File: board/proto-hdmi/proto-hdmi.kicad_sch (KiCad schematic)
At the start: 38 parts, among them J1 Conn_02x17_Odd_Even, J2 HDMI_A_1.4

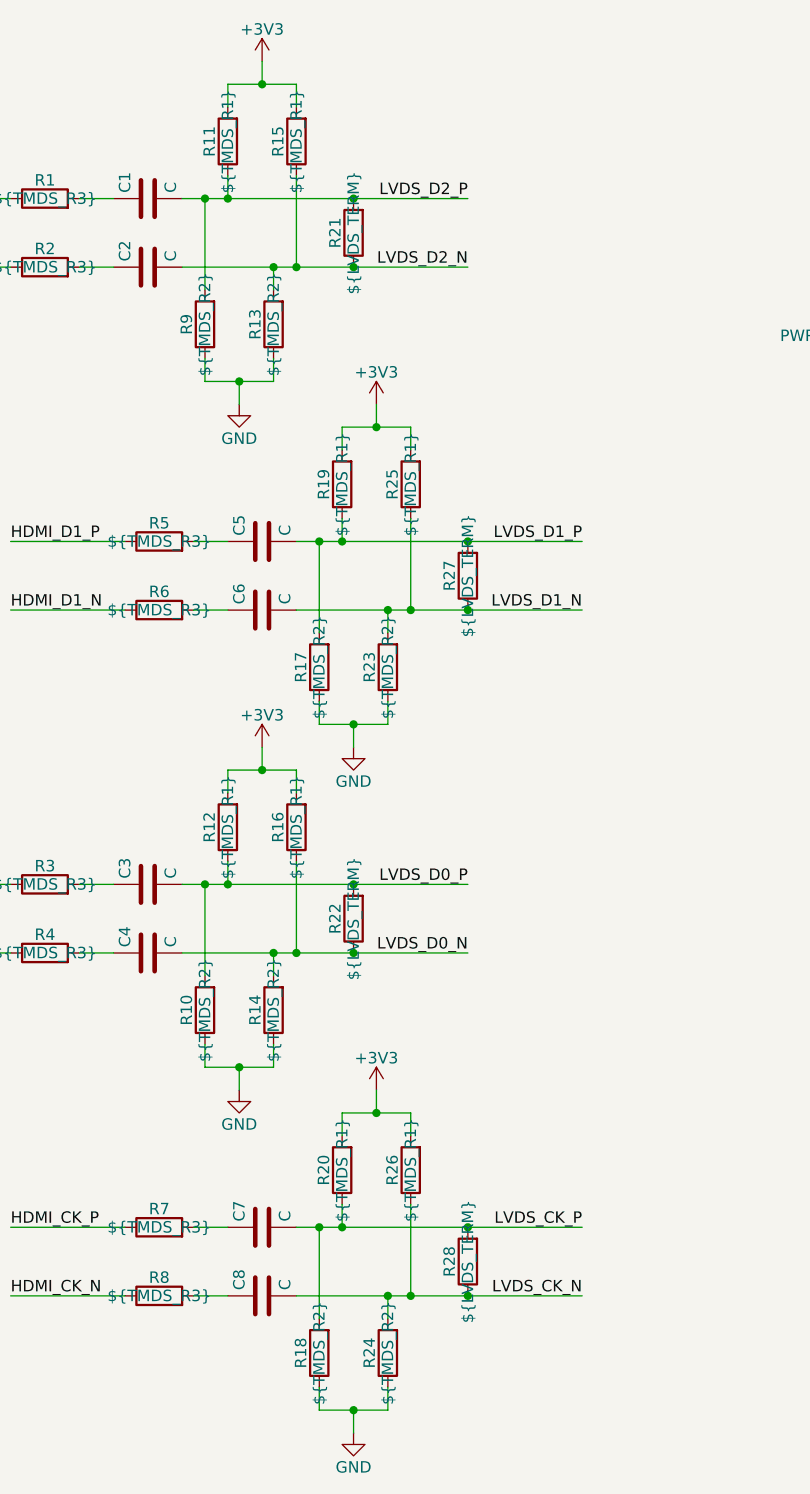
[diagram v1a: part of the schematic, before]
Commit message: Remove extraneous LVDS termination resistors.
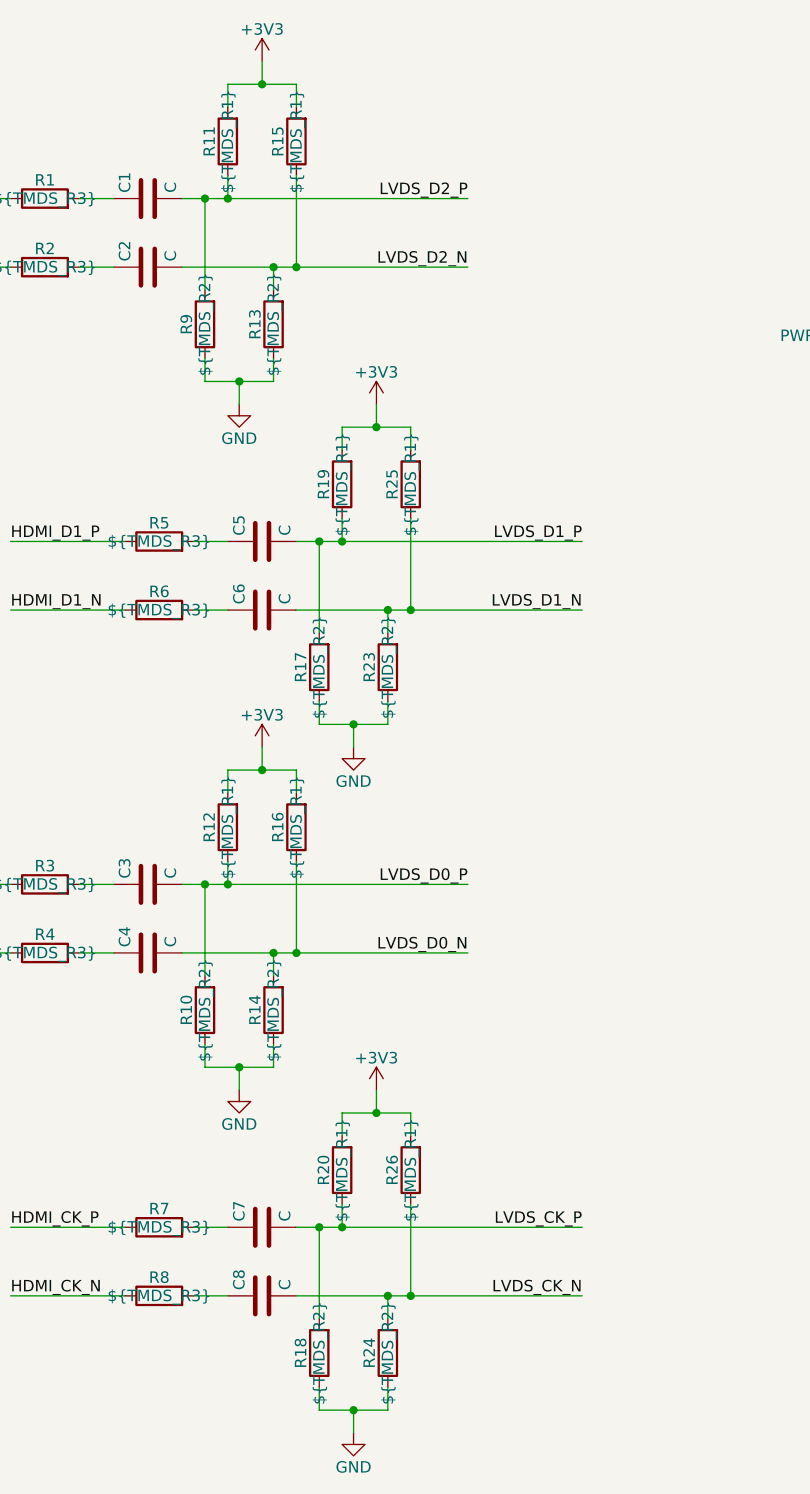
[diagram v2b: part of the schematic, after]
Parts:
- removed R21, R22, R27, R28: ${LVDS_TERM}, Resistor_SMD:R_0402_1005Metric, symbol Device:R
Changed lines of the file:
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@@
     (comment 1 "https://github.com/Elemecca/1240pi")
   )
-  (junction (at 152.4 83.82) (diameter 0) (color 0 0 0 0)
-  )
-  (junction (at 152.4 152.4) (diameter 0) (color 0 0 0 0)
-  )
   (junction (at 142.24 63.5) (diameter 0) (color 0 0 0 0)
   )
@@
   (junction (at 143.51 160.02) (diameter 0) (color 0 0 0 0)
   )
-  (junction (at 139.7 121.92) (diameter 0) (color 0 0 0 0)
-  )
   (junction (at 123.19 38.1) (diameter 0) (color 0 0 0 0)
   )
@@
   (junction (at 138.43 76.2) (diameter 0) (color 0 0 0 0)
   )
-  (junction (at 139.7 38.1) (diameter 0) (color 0 0 0 0)
-  )
   (junction (at 135.89 76.2) (diameter 0) (color 0 0 0 0)
   )
@@
   (junction (at 139.7 172.72) (diameter 0) (color 0 0 0 0)
   )
-  (junction (at 152.4 76.2) (diameter 0) (color 0 0 0 0)
-  )
   (junction (at 123.19 114.3) (diameter 0) (color 0 0 0 0)
   )
   (junction (at 139.7 96.52) (diameter 0) (color 0 0 0 0)
   )
-  (junction (at 139.7 114.3) (diameter 0) (color 0 0 0 0)
-  )
   (junction (at 207.01 59.69) (diameter 0) (color 0 0 0 0)
   )
@@
   (junction (at 138.43 152.4) (diameter 0) (color 0 0 0 0)
   )
-  (junction (at 152.4 160.02) (diameter 0) (color 0 0 0 0)
-  )
   (junction (at 44.45 106.68) (diameter 0) (color 0 0 0 0)
   )
   (junction (at 36.83 106.68) (diameter 0) (color 0 0 0 0)
-  )
-  (junction (at 139.7 45.72) (diameter 0) (color 0 0 0 0)
   )
   (junction (at 39.37 106.68) (diameter 0) (color 0 0 0 0)
@@
     (stroke (width 0) (type default) (color 0 0 0 0))
   )
-  (wire (pts (xy 139.7 121.92) (xy 152.4 121.92))
+  (wire (pts (xy 133.35 121.92) (xy 152.4 121.92))
     (stroke (width 0) (type default) (color 0 0 0 0))
   )
@@
     (stroke (width 0) (type default) (color 0 0 0 0))
   )
-  (wire (pts (xy 152.4 83.82) (xy 165.1 83.82))
+  (wire (pts (xy 146.05 83.82) (xy 165.1 83.82))
     (stroke (width 0) (type default) (color 0 0 0 0))
   )
@@
     (stroke (width 0) (type default) (color 0 0 0 0))
   )
-  (wire (pts (xy 133.35 121.92) (xy 139.7 121.92))
-    (stroke (width 0) (type default) (color 0 0 0 0))
-  )
   (wire (pts (xy 138.43 149.86) (xy 138.43 152.4))
     (stroke (width 0) (type default) (color 0 0 0 0))
@@
     (stroke (width 0) (type default) (color 0 0 0 0))
   )
-  (wire (pts (xy 152.4 152.4) (xy 165.1 152.4))
-    (stroke (width 0) (type default) (color 0 0 0 0))
-  )
   (wire (pts (xy 146.05 63.5) (xy 146.05 66.04))
     (stroke (width 0) (type default) (color 0 0 0 0))
   )
-  (wire (pts (xy 139.7 38.1) (xy 152.4 38.1))
+  (wire (pts (xy 125.73 38.1) (xy 152.4 38.1))
     (stroke (width 0) (type default) (color 0 0 0 0))
   )
@@
     (stroke (width 0) (type default) (color 0 0 0 0))
   )
-  (wire (pts (xy 146.05 160.02) (xy 152.4 160.02))
+  (wire (pts (xy 146.05 160.02) (xy 165.1 160.02))
     (stroke (width 0) (type default) (color 0 0 0 0))
   )
@@
     (stroke (width 0) (type default) (color 0 0 0 0))
   )
-  (wire (pts (xy 139.7 114.3) (xy 152.4 114.3))
+  (wire (pts (xy 125.73 114.3) (xy 152.4 114.3))
     (stroke (width 0) (type default) (color 0 0 0 0))
   )
@@
     (stroke (width 0) (type default) (color 0 0 0 0))
   )
-  (wire (pts (xy 125.73 38.1) (xy 139.7 38.1))
-    (stroke (width 0) (type default) (color 0 0 0 0))
-  )
   (wire (pts (xy 135.89 152.4) (xy 138.43 152.4))
     (stroke (width 0) (type default) (color 0 0 0 0))
@@
     (stroke (width 0) (type default) (color 0 0 0 0))
   )
-  (wire (pts (xy 146.05 83.82) (xy 152.4 83.82))
-    (stroke (width 0) (type default) (color 0 0 0 0))
-  )
   (wire (pts (xy 135.89 76.2) (xy 135.89 86.36))
     (stroke (width 0) (type default) (color 0 0 0 0))
@@
     (stroke (width 0) (type default) (color 0 0 0 0))
   )
-  (wire (pts (xy 138.43 76.2) (xy 152.4 76.2))
-    (stroke (width 0) (type default) (color 0 0 0 0))
-  )
   (wire (pts (xy 215.9 57.15) (xy 215.9 59.69))
     (stroke (width 0) (type default) (color 0 0 0 0))
@@
     (stroke (width 0) (type default) (color 0 0 0 0))
   )
-  (wire (pts (xy 152.4 160.02) (xy 165.1 160.02))
-    (stroke (width 0) (type default) (color 0 0 0 0))
-  )
   (wire (pts (xy 41.91 106.68) (xy 39.37 106.68))
     (stroke (width 0) (type default) (color 0 0 0 0))
@@
     (stroke (width 0) (type default) (color 0 0 0 0))
   )
-  (wire (pts (xy 133.35 45.72) (xy 139.7 45.72))
-    (stroke (width 0) (type default) (color 0 0 0 0))
-  )
   (wire (pts (xy 196.85 83.82) (xy 215.9 83.82))
     (stroke (width 0) (type default) (color 0 0 0 0))
@@
     (stroke (width 0) (type default) (color 0 0 0 0))
   )
-  (wire (pts (xy 138.43 152.4) (xy 152.4 152.4))
+  (wire (pts (xy 138.43 152.4) (xy 165.1 152.4))
     (stroke (width 0) (type default) (color 0 0 0 0))
   )
@@
     (stroke (width 0) (type default) (color 0 0 0 0))
   )
-  (wire (pts (xy 152.4 76.2) (xy 165.1 76.2))
+  (wire (pts (xy 138.43 76.2) (xy 165.1 76.2))
     (stroke (width 0) (type default) (color 0 0 0 0))
   )
@@
     (stroke (width 0) (type default) (color 0 0 0 0))
   )
-  (wire (pts (xy 125.73 114.3) (xy 139.7 114.3))
-    (stroke (width 0) (type default) (color 0 0 0 0))
-  )
   (wire (pts (xy 196.85 96.52) (xy 215.9 96.52))
     (stroke (width 0) (type default) (color 0 0 0 0))
@@
     (stroke (width 0) (type default) (color 0 0 0 0))
   )
-  (wire (pts (xy 139.7 45.72) (xy 152.4 45.72))
+  (wire (pts (xy 133.35 45.72) (xy 152.4 45.72))
     (stroke (width 0) (type default) (color 0 0 0 0))
   )
@@
     (pin "2")
   )
-  (symbol (lib_id "Device:R") (at 139.7 118.11 180) (unit 1)
-    (in_bom yes) (on_board yes)
-    (property "Reference" "R22" (id 0) (at 137.668 118.11 90))
-    (property "Value" "${LVDS_TERM}" (id 1) (at 139.7 118.11 90))
-    (property "Footprint" "Resistor_SMD:R_0402_1005Metric" (id 2) (at 141.478 118.11 90)
-      (effects (font (size 1.27 1.27)) hide)
-    )
-    (property "Datasheet" "~" (id 3) (at 139.7 118.11 0)
-      (effects (font (size 1.27 1.27)) hide)
-    )
-    (pin "1")
-    (pin "2")
-  )
   (symbol (lib_id "Device:R") (at 135.89 90.17 180) (unit 1)
     (in_bom yes) (on_board yes)
@@
     (pin "1")
   )
-  (symbol (lib_id "Device:R") (at 152.4 80.01 180) (unit 1)
-    (in_bom yes) (on_board yes)
-    (property "Reference" "R27" (id 0) (at 150.368 80.01 90))
-    (property "Value" "${LVDS_TERM}" (id 1) (at 152.4 80.01 90))
-    (property "Footprint" "Resistor_SMD:R_0402_1005Metric" (id 2) (at 154.178 80.01 90)
-      (effects (font (size 1.27 1.27)) hide)
-    )
-    (property "Datasheet" "~" (id 3) (at 152.4 80.01 0)
-      (effects (font (size 1.27 1.27)) hide)
-    )
-    (pin "1")
-    (pin "2")
-  )
   (symbol (lib_id "Device:R") (at 105.41 45.72 90) (unit 1)
     (in_bom yes) (on_board yes)
@@
     )
     (property "Datasheet" "~" (id 3) (at 129.54 83.82 0)
-      (effects (font (size 1.27 1.27)) hide)
-    )
-    (pin "1")
-    (pin "2")
-  )
-  (symbol (lib_id "Device:R") (at 139.7 41.91 180) (unit 1)
-    (in_bom yes) (on_board yes)
-    (property "Reference" "R21" (id 0) (at 137.668 41.91 90))
-    (property "Value" "${LVDS_TERM}" (id 1) (at 139.7 41.91 90))
-    (property "Footprint" "Resistor_SMD:R_0402_1005Metric" (id 2) (at 141.478 41.91 90)
-      (effects (font (size 1.27 1.27)) hide)
-    )
-    (property "Datasheet" "~" (id 3) (at 139.7 41.91 0)
       (effects (font (size 1.27 1.27)) hide)
     )
@@
     )
     (pin "1")
-  )
-  (symbol (lib_id "Device:R") (at 152.4 156.21 180) (unit 1)
-    (in_bom yes) (on_board yes)
-    (property "Reference" "R28" (id 0) (at 150.368 156.21 90))
-    (property "Value" "${LVDS_TERM}" (id 1) (at 152.4 156.21 90))
-    (property "Footprint" "Resistor_SMD:R_0402_1005Metric" (id 2) (at 154.178 156.21 90)
-      (effects (font (size 1.27 1.27)) hide)
-    )
-    (property "Datasheet" "~" (id 3) (at 152.4 156.21 0)
-      (effects (font (size 1.27 1.27)) hide)
-    )
-    (pin "1")
-    (pin "2")
   )
   (symbol (lib_id "Connector_Generic:Conn_02x17_Odd_Even") (at 220.98 83.82 0) (unit 1)
@@
       (reference "R20") (unit 1) (value "${TMDS_R1}") (footprint "Resistor_SMD:R_0402_1005Metric")
     )
-    (path "/4042c566-dbe0-4fcc-a8e6-2f9abdb810bb"
-      (reference "R21") (unit 1) (value "${LVDS_TERM}") (footprint "Resistor_SMD:R_0402_1005Metric")
-    )
-    (path "/104e9296-e4eb-4e51-9155-4c6635c6dad8"
-      (reference "R22") (unit 1) (value "${LVDS_TERM}") (footprint "Resistor_SMD:R_0402_1005Metric")
-    )
     (path "/3ac8a9ee-2153-4f97-8d54-eee8368f298d"
       (reference "R23") (unit 1) (value "${TMDS_R2}") (footprint "Resistor_SMD:R_0402_1005Metric")
@@
       (reference "R26") (unit 1) (value "${TMDS_R1}") (footprint "Resistor_SMD:R_0402_1005Metric")
     )
-    (path "/2095c295-4164-4ab7-b0cf-247827021489"
-      (reference "R27") (unit 1) (value "${LVDS_TERM}") (footprint "Resistor_SMD:R_0402_1005Metric")
-    )
-    (path "/782a149a-c296-4cfa-8045-5d14501481ec"
-      (reference "R28") (unit 1) (value "${LVDS_TERM}") (footprint "Resistor_SMD:R_0402_1005Metric")
-    )
-  )
+  )

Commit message: Add labels to HDMI board.
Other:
- title: HDMI Adapter for Lattice ICE40HX8K-B-EVN -> HDMI Expansion for Olimex ICE40HX8K-EVB
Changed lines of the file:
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@@
   (paper "USLetter")
   (title_block
-    (title "HDMI Adapter for Lattice ICE40HX8K-B-EVN")
+    (title "HDMI Expansion for Olimex ICE40HX8K-EVB")
     (date "2022-04-19")
-    (rev "1.0")
+    (rev "0.1")
     (company "© 2022 Sam Hanes, licensed under CERN-OHL-P v2")
     (comment 1 "https://github.com/Elemecca/1240pi")

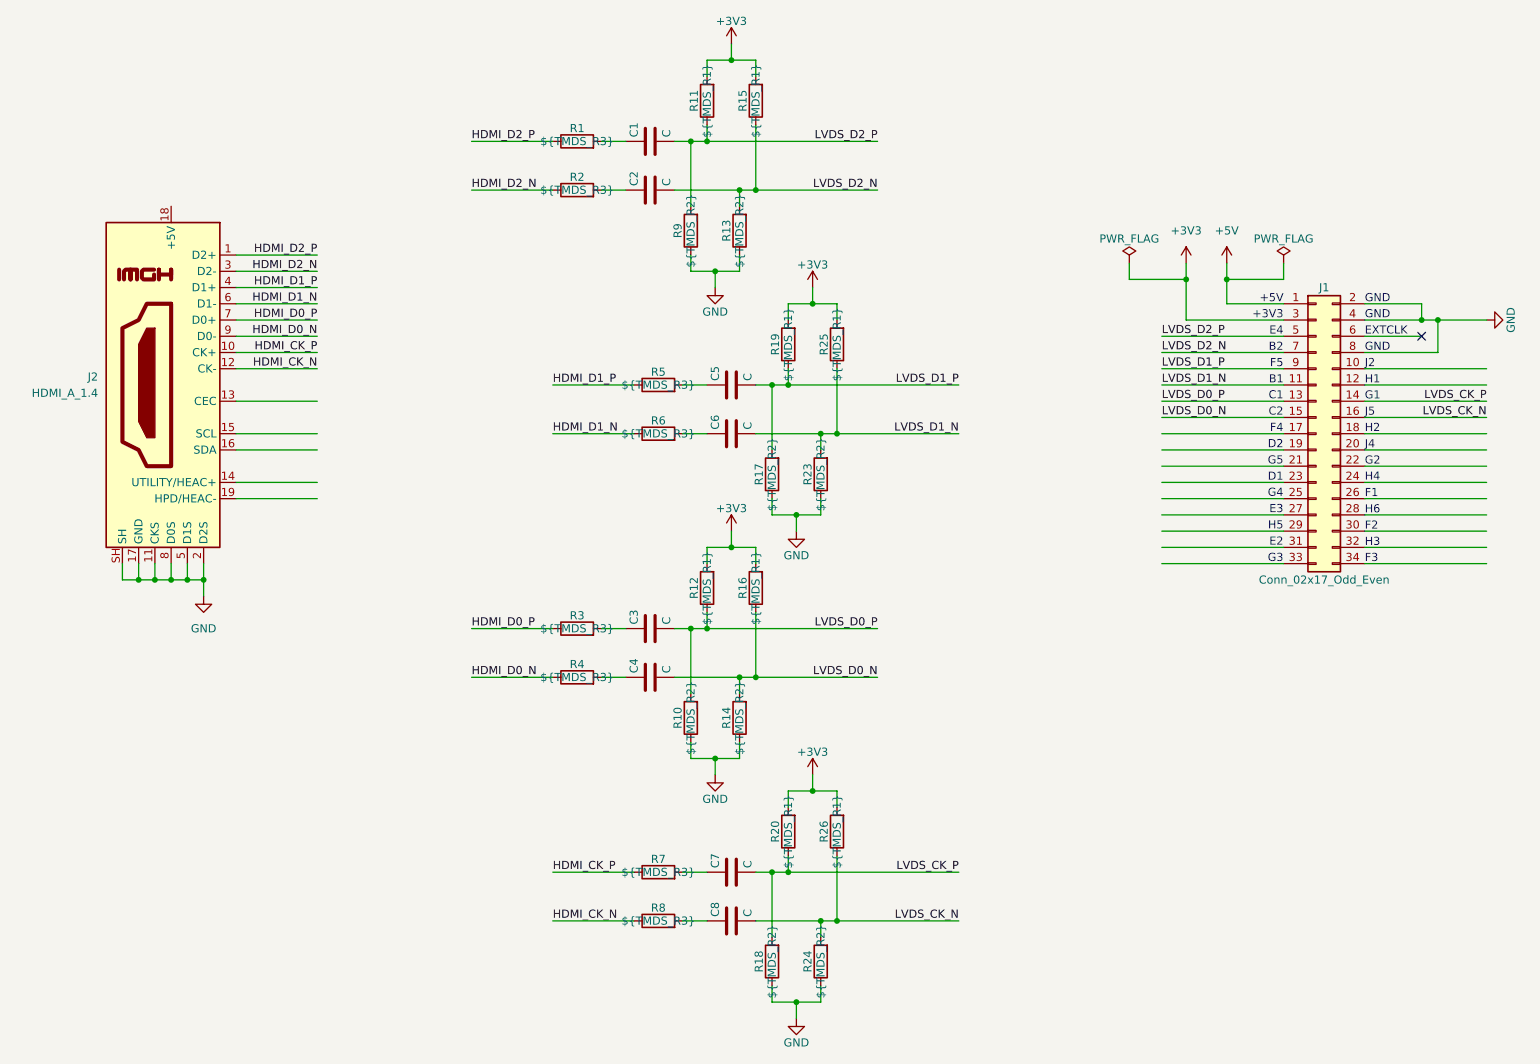
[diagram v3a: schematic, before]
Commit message: Add and route non-TMDS lines for sink port.
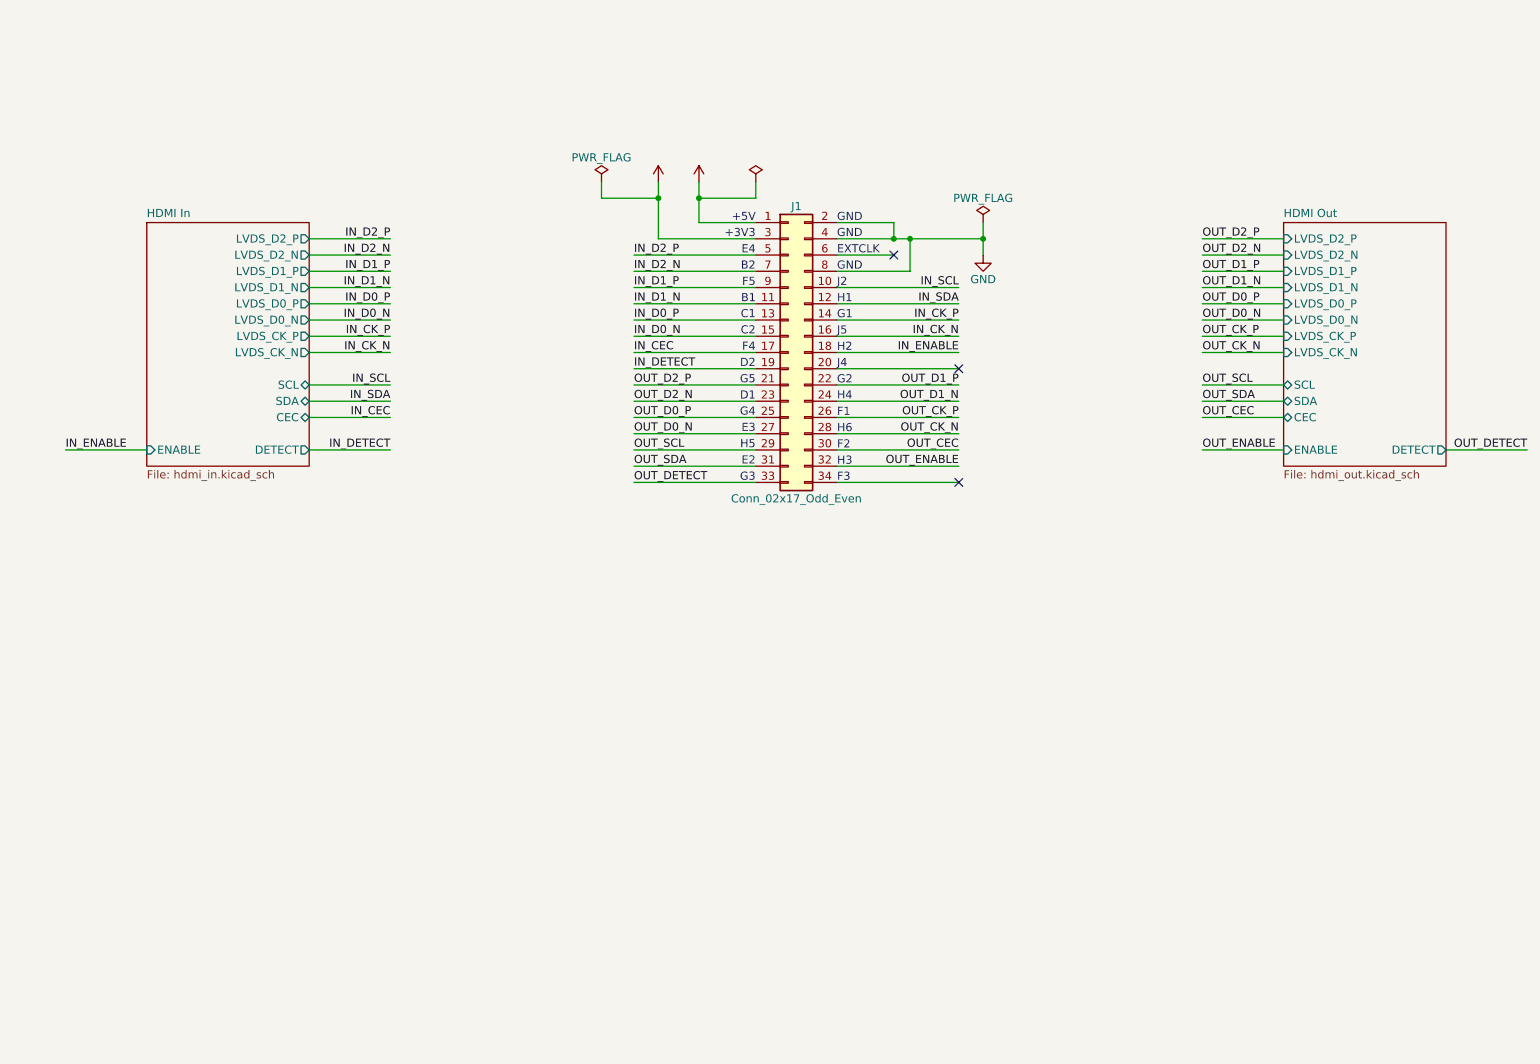
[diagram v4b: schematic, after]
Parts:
- removed C1, C2, C3, C4, C5, C6, C7, C8: C, Capacitor_SMD:C_0402_1005Metric, symbol Device:C
- removed J2: HDMI_A_1.4, 0Local:CNC_2000-1-2-41-00-BK, symbol Connector:HDMI_A_1.4
- removed R1, R2, R3, R4, R5, R6, R7, R8: ${TMDS_R3}, Resistor_SMD:R_0402_1005Metric, symbol Device:R
- removed R10, R13, R14, R17, R18, R23, R24, R9: ${TMDS_R2}, Resistor_SMD:R_0402_1005Metric, symbol Device:R
- removed R11, R12, R15, R16, R19, R20, R25, R26: ${TMDS_R1}, Resistor_SMD:R_0402_1005Metric, symbol Device:R
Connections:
- net IN_SCL: now reaches J1.10 (Pin_10)
- net IN_SDA: now reaches J1.12 (Pin_12)
- net IN_CEC: now reaches J1.17 (Pin_17)
- net IN_ENABLE: now reaches J1.18 (Pin_18)
- net IN_DETECT: now reaches J1.19 (Pin_19)
- net OUT_D2_P: now reaches J1.21 (Pin_21)
- net OUT_D1_P: now reaches J1.22 (Pin_22)
- net OUT_D2_N: now reaches J1.23 (Pin_23)
- net OUT_D1_N: now reaches J1.24 (Pin_24)
- net OUT_D0_P: now reaches J1.25 (Pin_25)
- net OUT_CK_P: now reaches J1.26 (Pin_26)
- net OUT_D0_N: now reaches J1.27 (Pin_27)
- net OUT_CK_N: now reaches J1.28 (Pin_28)
- net OUT_SCL: now reaches J1.29 (Pin_29)
- net OUT_CEC: now reaches J1.30 (Pin_30)
- net OUT_SDA: now reaches J1.31 (Pin_31)
- net OUT_ENABLE: now reaches J1.32 (Pin_32)
- net OUT_DETECT: now reaches J1.33 (Pin_33)
- net LVDS_CK_N renamed IN_CK_N
- net LVDS_CK_P renamed IN_CK_P
- net LVDS_D0_N renamed IN_D0_N
- net LVDS_D0_P renamed IN_D0_P
- net LVDS_D1_N renamed IN_D1_N
- net LVDS_D1_P renamed IN_D1_P
- net LVDS_D2_N renamed IN_D2_N
- net LVDS_D2_P renamed IN_D2_P
- no-connect marks 1 -> 3
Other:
- added sheet HDMI In (hdmi_in.kicad_sch)
- added sheet HDMI Out (hdmi_out.kicad_sch)
- moved on the sheet: J1
